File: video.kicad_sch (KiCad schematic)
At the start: 5 parts, among them J4 DB9FEM, P1 BNC, P2 BNC, P3 BNC, P8 BNC

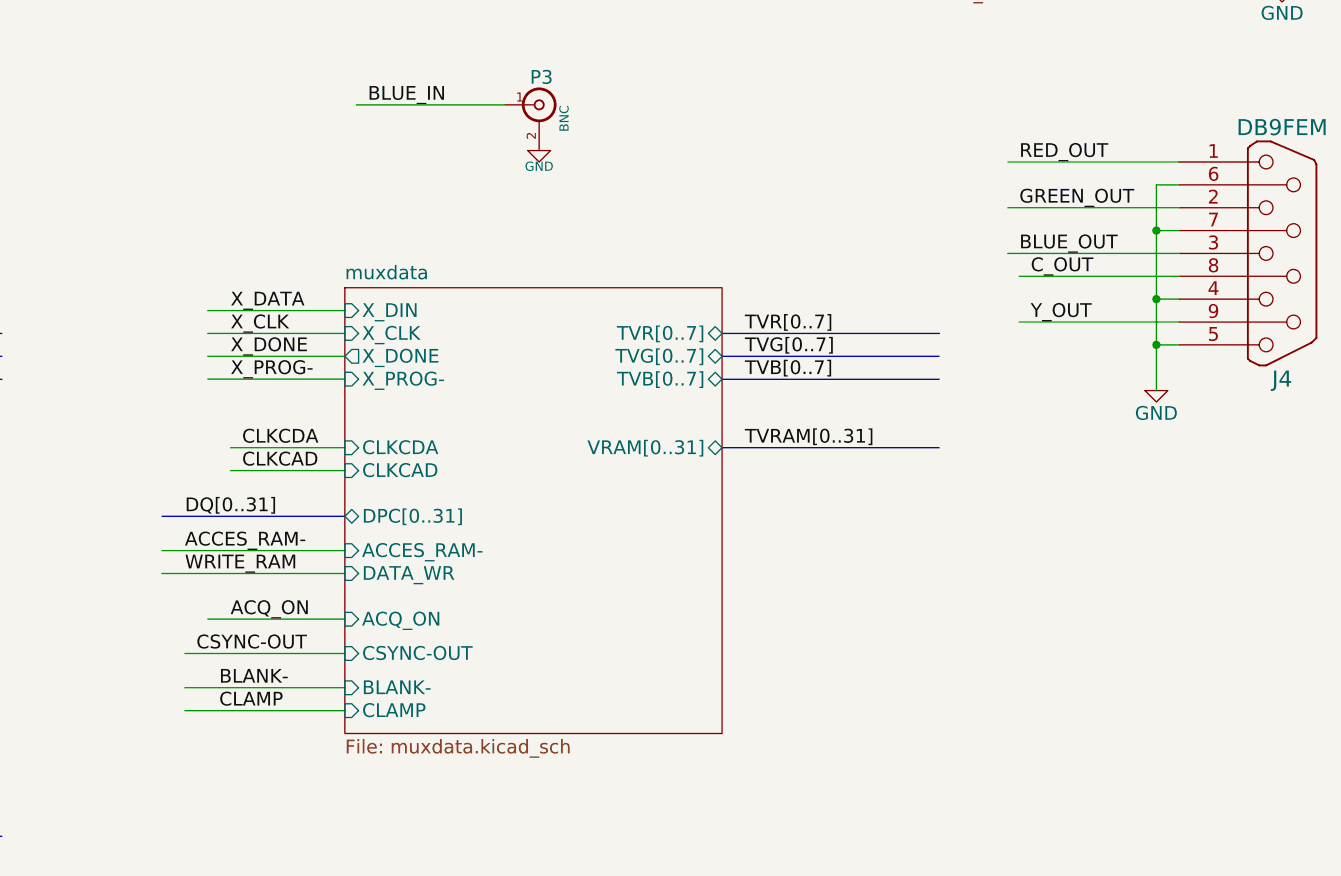
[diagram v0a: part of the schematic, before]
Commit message: update to kicad 9
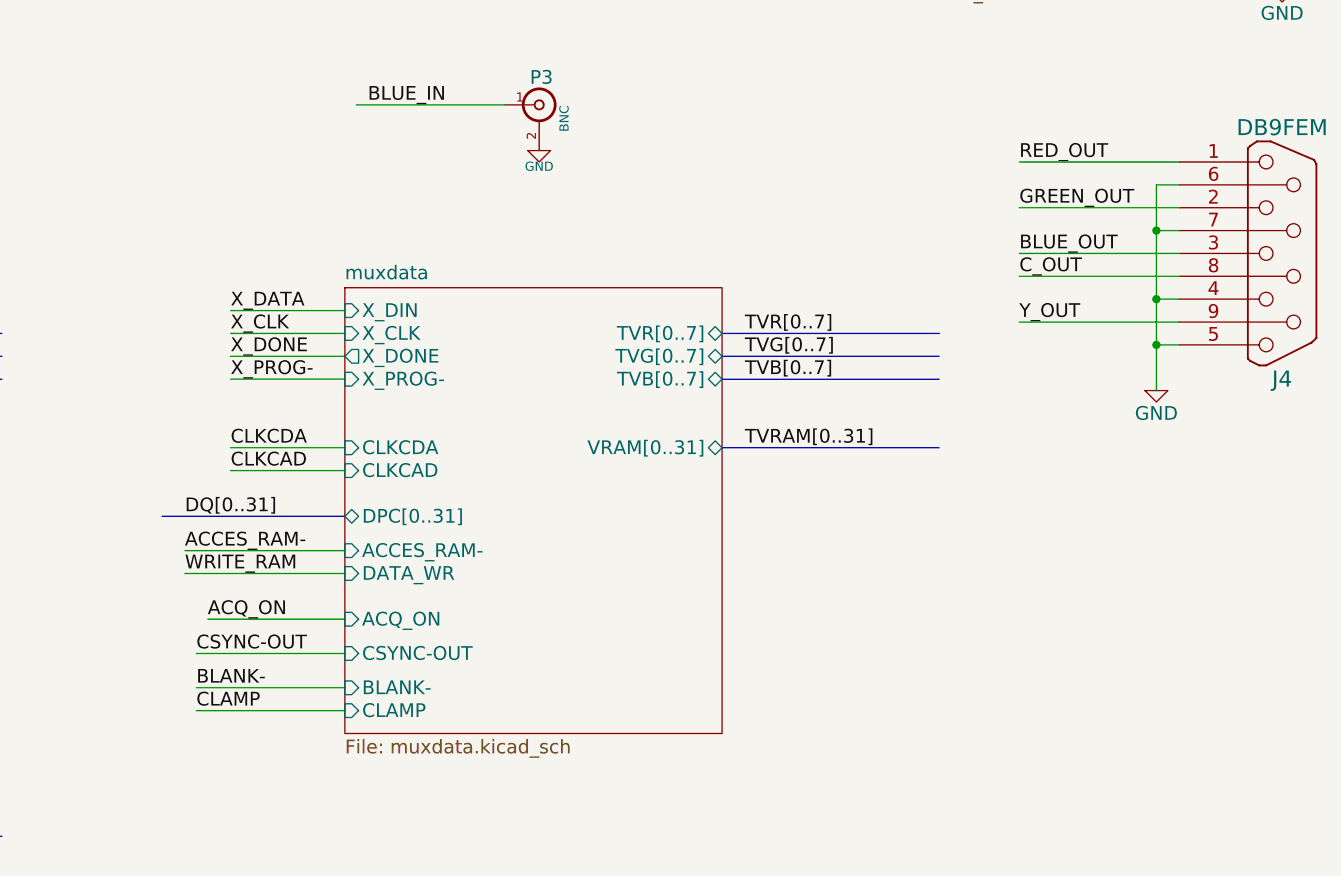
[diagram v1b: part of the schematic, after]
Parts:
- P1, P2, P3, P8: footprint Discret:SUBCLICK -> footprints:subclick
